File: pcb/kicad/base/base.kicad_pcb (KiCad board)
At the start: 2 copper layers, 59 parts, among them J1 CHIP_EN, J2 Vbatt_I-test, P1 J-Link SWD, P2 SMA, P3 Power Source, P4 CONN_01X08, U1 SAMB11G18A-edit, U2 XBee-PRO_900HP, Y1 32.768kHz, Y2 26MHz

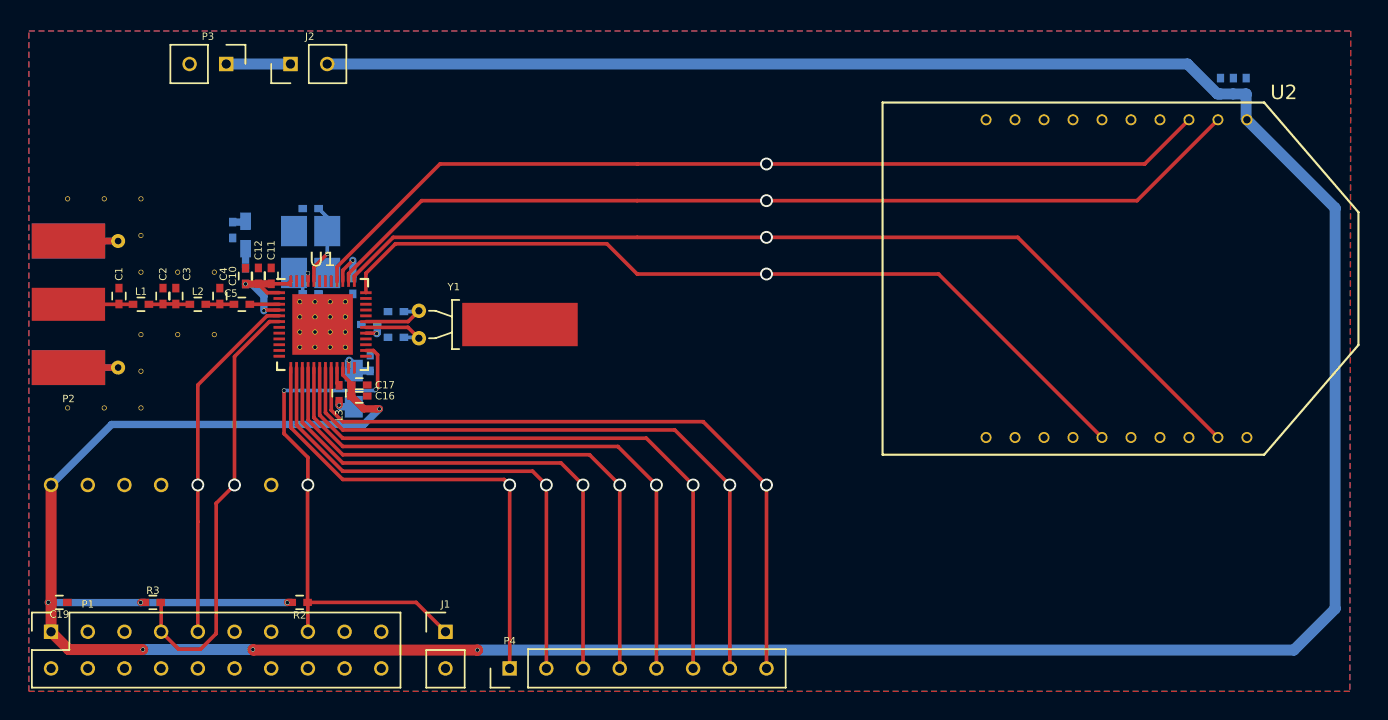
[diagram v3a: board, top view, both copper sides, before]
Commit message: Cleanup base schematic and layout
Power routes have been placed to completely cover the entire board.
Crystal adjusted slightly to avoid the UART TX signal line. More vias
dispersed around the board for better ground connections. Gerber files
have been created and are ready to be tiled.
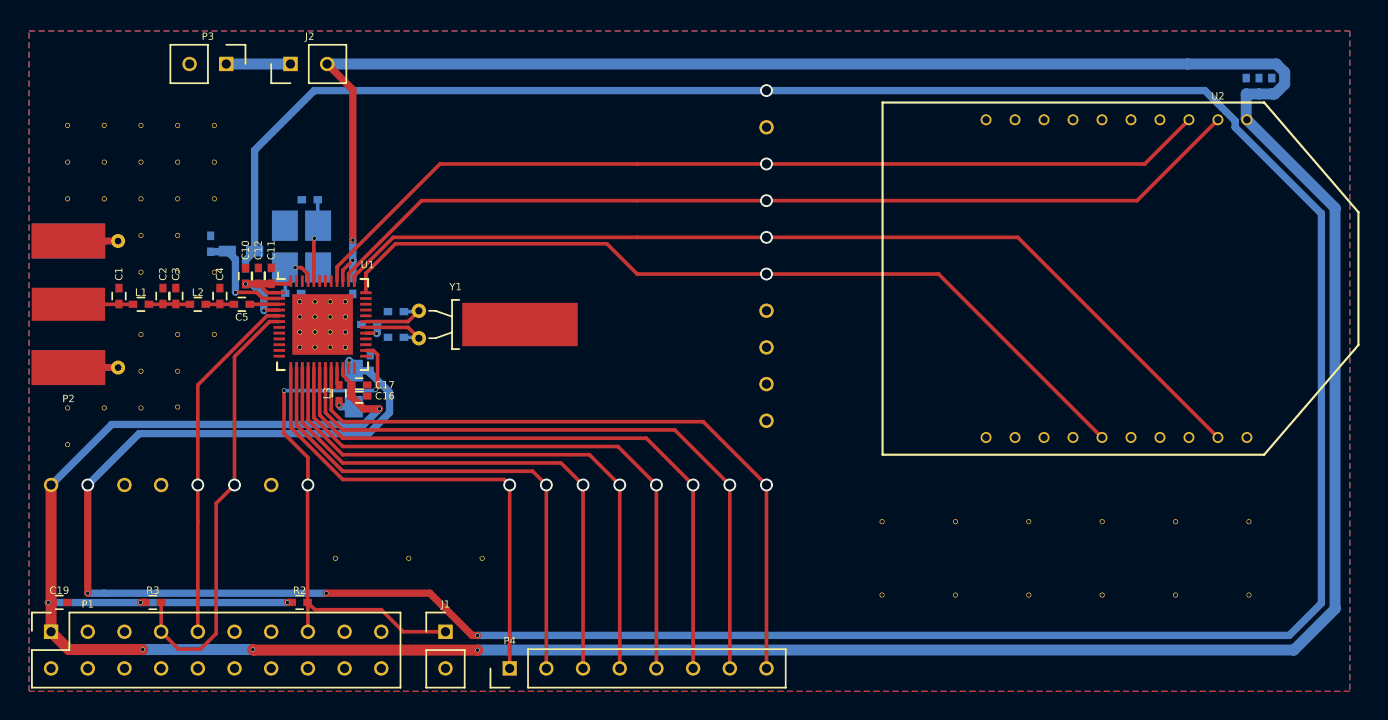
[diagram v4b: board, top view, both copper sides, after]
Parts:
- removed the REF** at (132.3, 100.0)
- added REF**: Via_Stitch_Dia0.356mm_Drill0.254mm, Misc:Via_Stitch_Dia0.356mm_Drill0.254mm, F.Cu at (138.6, 92.1)
- added REF**: Via_Stitch_Dia0.356mm_Drill0.254mm, Misc:Via_Stitch_Dia0.356mm_Drill0.254mm, F.Cu at (138.6, 94.6)
- added REF**: Via_Stitch_Dia0.356mm_Drill0.254mm, Misc:Via_Stitch_Dia0.356mm_Drill0.254mm, F.Cu at (138.6, 82.7)
- added REF**: Via_Stitch_Dia0.356mm_Drill0.254mm, Misc:Via_Stitch_Dia0.356mm_Drill0.254mm, F.Cu at (138.6, 80.2)
- added REF**: Via_Stitch_Dia1.00mm_Drill0.64mm, Misc:Via_Stitch_Dia1.00mm_Drill0.64mm, F.Cu at (179.3, 75.2)
- added REF**: Via_Stitch_Dia1.00mm_Drill0.64mm, Misc:Via_Stitch_Dia1.00mm_Drill0.64mm, F.Cu at (179.3, 87.9)
- added REF**: Via_Stitch_Dia1.00mm_Drill0.64mm, Misc:Via_Stitch_Dia1.00mm_Drill0.64mm, F.Cu at (179.3, 90.5)
- added REF**: Via_Stitch_Dia0.356mm_Drill0.254mm, Misc:Via_Stitch_Dia0.356mm_Drill0.254mm, F.Cu at (130.9, 97.2)
- added REF**: Via_Stitch_Dia0.356mm_Drill0.254mm, Misc:Via_Stitch_Dia0.356mm_Drill0.254mm, F.Cu at (130.9, 77.7)
- added REF**: Via_Stitch_Dia0.356mm_Drill0.254mm, Misc:Via_Stitch_Dia0.356mm_Drill0.254mm, F.Cu at (133.5, 77.7)
- added REF**: Via_Stitch_Dia0.356mm_Drill0.254mm, Misc:Via_Stitch_Dia0.356mm_Drill0.254mm, F.Cu at (136.0, 77.7)
- added REF**: Via_Stitch_Dia0.356mm_Drill0.254mm, Misc:Via_Stitch_Dia0.356mm_Drill0.254mm, F.Cu at (138.6, 77.7)
- added REF**: Via_Stitch_Dia0.356mm_Drill0.254mm, Misc:Via_Stitch_Dia0.356mm_Drill0.254mm, F.Cu at (141.1, 80.2)
- added REF**: Via_Stitch_Dia0.356mm_Drill0.254mm, Misc:Via_Stitch_Dia0.356mm_Drill0.254mm, F.Cu at (141.1, 77.7)
- added REF**: Via_Stitch_Dia0.356mm_Drill0.254mm, Misc:Via_Stitch_Dia0.356mm_Drill0.254mm, F.Cu at (130.9, 75.1)
- added REF**: Via_Stitch_Dia0.356mm_Drill0.254mm, Misc:Via_Stitch_Dia0.356mm_Drill0.254mm, F.Cu at (133.5, 75.1)
- added REF**: Via_Stitch_Dia0.356mm_Drill0.254mm, Misc:Via_Stitch_Dia0.356mm_Drill0.254mm, F.Cu at (136.0, 75.1)
- added REF**: Via_Stitch_Dia0.356mm_Drill0.254mm, Misc:Via_Stitch_Dia0.356mm_Drill0.254mm, F.Cu at (138.6, 75.1)
- added REF**: Via_Stitch_Dia0.356mm_Drill0.254mm, Misc:Via_Stitch_Dia0.356mm_Drill0.254mm, F.Cu at (141.1, 75.1)
- added REF**: Via_Stitch_Dia1.00mm_Drill0.64mm, Misc:Via_Stitch_Dia1.00mm_Drill0.64mm, F.Cu at (179.3, 93.0)
- added REF**: Via_Stitch_Dia1.00mm_Drill0.64mm, Misc:Via_Stitch_Dia1.00mm_Drill0.64mm, F.Cu at (179.3, 95.6)
- added REF**: Via_Stitch_Dia0.356mm_Drill0.254mm, Misc:Via_Stitch_Dia0.356mm_Drill0.254mm, F.Cu at (187.3, 107.6)
- added REF**: Via_Stitch_Dia0.356mm_Drill0.254mm, Misc:Via_Stitch_Dia0.356mm_Drill0.254mm, F.Cu at (192.4, 107.6)
- added REF**: Via_Stitch_Dia0.356mm_Drill0.254mm, Misc:Via_Stitch_Dia0.356mm_Drill0.254mm, F.Cu at (197.5, 107.6)
- added REF**: Via_Stitch_Dia0.356mm_Drill0.254mm, Misc:Via_Stitch_Dia0.356mm_Drill0.254mm, F.Cu at (202.6, 107.6)
- added REF**: Via_Stitch_Dia0.356mm_Drill0.254mm, Misc:Via_Stitch_Dia0.356mm_Drill0.254mm, F.Cu at (207.6, 107.6)
- added REF**: Via_Stitch_Dia0.356mm_Drill0.254mm, Misc:Via_Stitch_Dia0.356mm_Drill0.254mm, F.Cu at (212.7, 107.6)
- added REF**: Via_Stitch_Dia0.356mm_Drill0.254mm, Misc:Via_Stitch_Dia0.356mm_Drill0.254mm, F.Cu at (187.3, 102.6)
- added REF**: Via_Stitch_Dia0.356mm_Drill0.254mm, Misc:Via_Stitch_Dia0.356mm_Drill0.254mm, F.Cu at (192.4, 102.6)
- added REF**: Via_Stitch_Dia0.356mm_Drill0.254mm, Misc:Via_Stitch_Dia0.356mm_Drill0.254mm, F.Cu at (197.5, 102.6)
- added REF**: Via_Stitch_Dia0.356mm_Drill0.254mm, Misc:Via_Stitch_Dia0.356mm_Drill0.254mm, F.Cu at (202.6, 102.6)
- added REF**: Via_Stitch_Dia0.356mm_Drill0.254mm, Misc:Via_Stitch_Dia0.356mm_Drill0.254mm, F.Cu at (207.6, 102.6)
- added REF**: Via_Stitch_Dia0.356mm_Drill0.254mm, Misc:Via_Stitch_Dia0.356mm_Drill0.254mm, F.Cu at (212.7, 102.6)
- added REF**: Via_Stitch_Dia0.356mm_Drill0.254mm, Misc:Via_Stitch_Dia0.356mm_Drill0.254mm, F.Cu at (149.5, 105.1)
- added REF**: Via_Stitch_Dia0.356mm_Drill0.254mm, Misc:Via_Stitch_Dia0.356mm_Drill0.254mm, F.Cu at (154.6, 105.1)
- added REF**: Via_Stitch_Dia0.356mm_Drill0.254mm, Misc:Via_Stitch_Dia0.356mm_Drill0.254mm, F.Cu at (159.6, 105.1)
- moved C22 3.56 mm to (214.3, 72.4)
- moved C13 1.80 mm to (140.8, 83.3), turned to 90 degrees
- moved C21 1.78 mm to (213.4, 72.4)
- moved C9 1.21 mm to (146.6, 86.7)
- moved FB1 1.16 mm to (142.9, 83.8), turned to 180 degrees
- moved Y2 0.74 mm to (147.1, 83.5)
- moved C8 0.61 mm to (147.7, 80.3)
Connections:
- net /LP_GPIO_2 renamed Net-(U1-Pad7)
- net /LP_GPIO_22 renamed Net-(U1-Pad10)
- net /LP_GPIO_23 renamed Net-(U1-Pad11)
- net /LP_GPIO_3 renamed Net-(U1-Pad8)
- net /LP_GPIO_4 renamed Net-(U1-Pad9)
- net /LP_GPIO_5 renamed Net-(U1-Pad12)
- U1 pad 41: /LP_GPIO_18 -> GND
- U1 pad 42: /LP_GPIO_19 -> GND
- U1 pad 43: /LP_GPIO_20 -> GND
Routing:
- net Net-(C14-Pad1): track 3.89 -> 238.7 mm, vias 1 -> 6
- net /+3.3V: track 253.3 -> 273.4 mm, vias 8 -> 9
- net Net-(C13-Pad1): track 0.91 -> 7.46 mm, vias 0 -> 1
- net Net-(C9-Pad1): track 3.21 -> 4.08 mm
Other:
- rule pad_to_mask_clearance: 0.2 -> 0.0762
- board text added: "0.1"
- board text removed: "1.0"

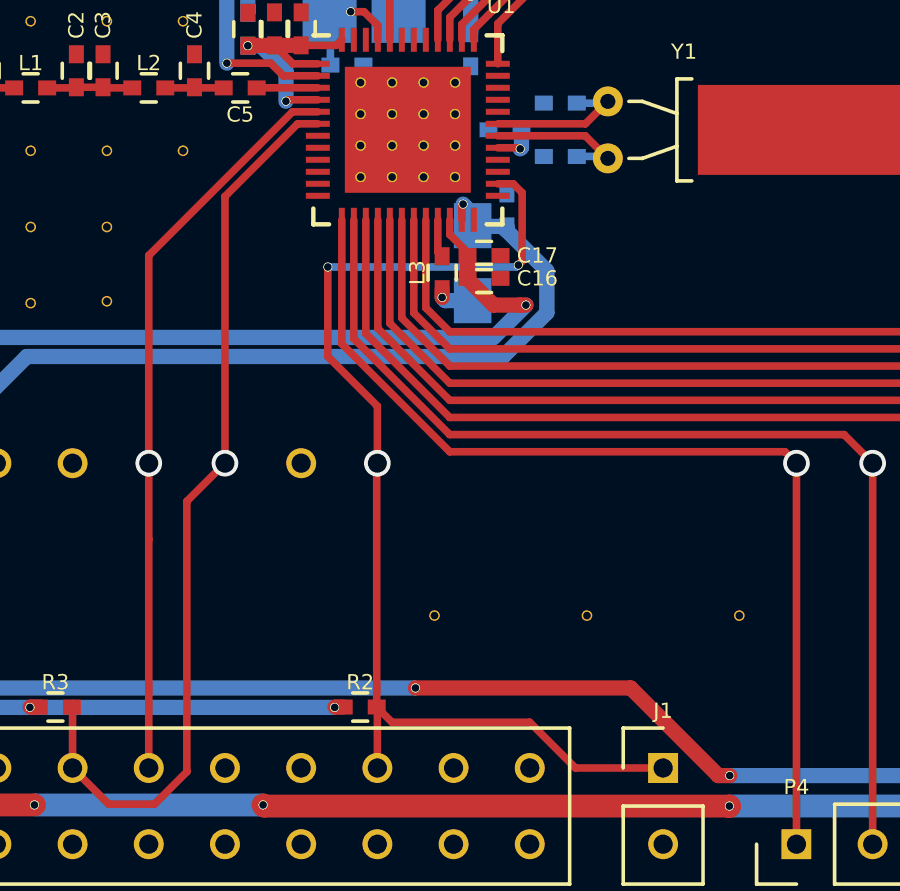
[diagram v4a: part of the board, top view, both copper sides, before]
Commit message: Fix annular ring clearance
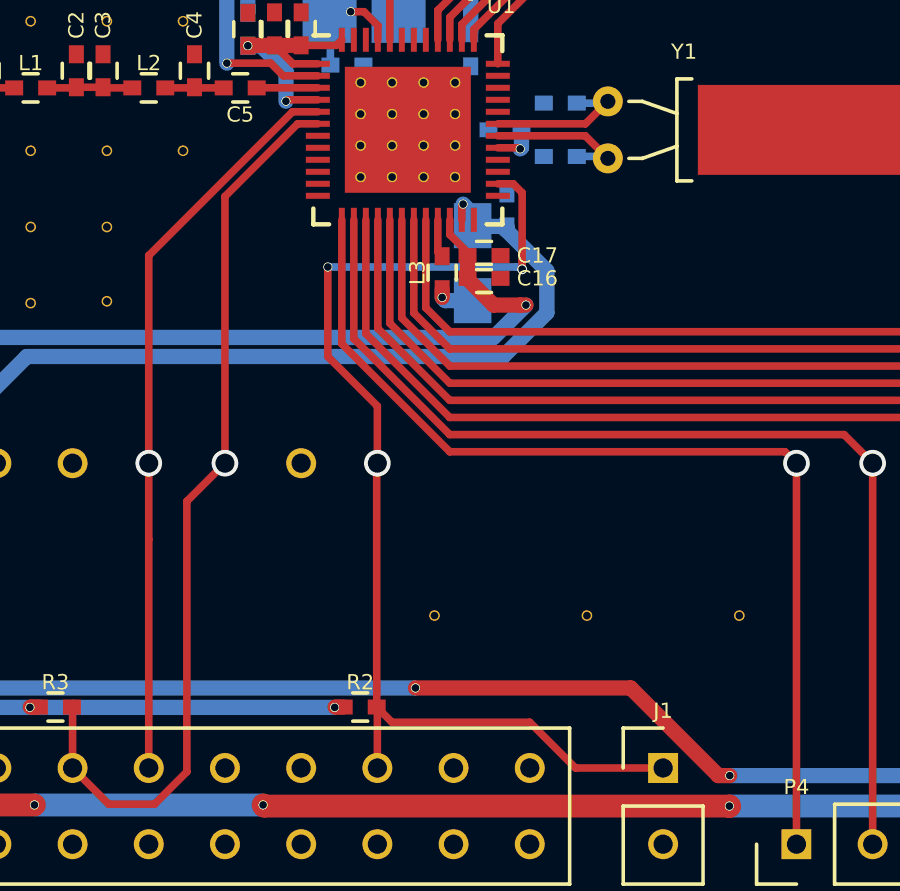
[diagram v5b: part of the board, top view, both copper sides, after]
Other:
- net class Default: via_dia 0.3048 -> 0.3302
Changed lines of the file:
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@@
-(kicad_pcb (version 4) (host pcbnew 4.0.5)
+(kicad_pcb (version 4) (host pcbnew 4.0.6)
   (general
     (links 200)
@@
     (thickness 1.6)
     (drawings 11)
-    (tracks 285)
+    (tracks 286)
     (zones 0)
     (modules 94)
@@
   )
   (setup
-    (last_trace_width 0.508)
+    (last_trace_width 0.254)
     (user_trace_width 0.508)
     (user_trace_width 0.762)
     (trace_clearance 0.127)
-    (zone_clearance 0.127)
+    (zone_clearance 0.1524)
     (zone_45_only yes)
     (trace_min 0.127)
     (segment_width 0.2)
     (edge_width 0.15)
-    (via_size 0.3048)
+    (via_size 0.3302)
     (via_drill 0.254)
     (via_min_size 0.254)
     (via_min_drill 0.254)
+    (user_via 0.3302 0.254)
     (user_via 0.889 0.635)
     (uvia_size 0.3)
@@
       (drillshape 0)
       (scaleselection 1)
-      (outputdirectory ""))
+      (outputdirectory artwork/))
   )
   (net 0 "")
@@
     (clearance 0.127)
     (trace_width 0.254)
-    (via_dia 0.3048)
+    (via_dia 0.3302)
     (via_drill 0.254)
     (uvia_dia 0.3)
@@
   (segment (start 149.84 94.595) (end 149.733 94.488) (width 0.508) (layer B.Cu) (net 45))
   (segment (start 150.749 94.595) (end 149.84 94.595) (width 0.508) (layer B.Cu) (net 45))
+  (segment (start 152.4 93.2815) (end 152.4 93.5482) (width 0.254) (layer F.Cu) (net 52))
+  (via (at 152.4 93.5482) (size 0.3302) (drill 0.254) (layers F.Cu B.Cu) (net 52))
+  (segment (start 152.3238 93.472) (end 152.4 93.5482) (width 0.254) (layer B.Cu) (net 52))
+  (segment (start 152.2095 93.472) (end 152.3238 93.472) (width 0.254) (layer B.Cu) (net 52))
+  (segment (start 152.1045 90.7) (end 152.4 90.9955) (width 0.254) (layer F.Cu) (net 52))
+  (segment (start 152.4 90.9955) (end 152.4 93.2815) (width 0.254) (layer F.Cu) (net 52))
+  (segment (start 151.59 90.7) (end 152.1045 90.7) (width 0.254) (layer F.Cu) (net 52))
+  (segment (start 152.2095 93.472) (end 145.923 93.472) (width 0.254) (layer B.Cu) (net 52))
+  (segment (start 147.574 98.1075) (end 145.923 96.4565) (width 0.254) (layer F.Cu) (net 52))
+  (segment (start 145.923 96.4565) (end 145.923 93.472) (width 0.254) (layer F.Cu) (net 52))
+  (via (at 145.923 93.472) (size 0.3048) (drill 0.254) (layers F.Cu B.Cu) (net 52))
+  (segment (start 147.5525 100.034) (end 147.5525 108.1405) (width 0.254) (layer F.Cu) (net 52))
+  (via (at 147.574 100.0125) (size 0.889) (drill 0.635) (layers F.Cu B.Cu) (net 52))
+  (segment (start 147.5525 100.034) (end 147.574 100.0125) (width 0.254) (layer F.Cu) (net 52))
+  (segment (start 147.574 100.0125) (end 147.574 98.1075) (width 0.254) (layer F.Cu) (net 52))
   (segment (start 148.0605 108.6485) (end 147.5525 108.1405) (width 0.254) (layer F.Cu) (net 52))
   (segment (start 152.654 108.6485) (end 148.0605 108.6485) (width 0.254) (layer F.Cu) (net 52))
   (segment (start 154.178 110.1725) (end 152.654 108.6485) (width 0.254) (layer F.Cu) (net 52))
   (segment (start 157.099 110.1725) (end 154.178 110.1725) (width 0.254) (layer F.Cu) (net 52))
-  (segment (start 147.574 100.0125) (end 147.574 98.1075) (width 0.254) (layer F.Cu) (net 52))
-  (segment (start 147.5525 100.034) (end 147.574 100.0125) (width 0.254) (layer F.Cu) (net 52))
-  (via (at 147.574 100.0125) (size 0.889) (drill 0.635) (layers F.Cu B.Cu) (net 52))
-  (segment (start 147.5525 108.1405) (end 147.5525 100.034) (width 0.254) (layer F.Cu) (net 52))
-  (segment (start 152.1045 90.7) (end 152.4 90.9955) (width 0.254) (layer F.Cu) (net 52))
-  (segment (start 152.4 90.9955) (end 152.4 93.2815) (width 0.254) (layer F.Cu) (net 52))
-  (segment (start 152.4 93.2815) (end 152.273 93.4085) (width 0.254) (layer F.Cu) (net 52))
-  (via (at 152.273 93.4085) (size 0.3048) (drill 0.254) (layers F.Cu B.Cu) (net 52))
-  (segment (start 152.273 93.4085) (end 152.2095 93.472) (width 0.254) (layer B.Cu) (net 52))
-  (segment (start 152.2095 93.472) (end 145.923 93.472) (width 0.254) (layer B.Cu) (net 52))
-  (via (at 145.923 93.472) (size 0.3048) (drill 0.254) (layers F.Cu B.Cu) (net 52))
-  (segment (start 152.1045 90.7) (end 151.59 90.7) (width 0.254) (layer F.Cu) (net 52))
-  (segment (start 145.923 96.4565) (end 145.923 93.472) (width 0.254) (layer F.Cu) (net 52))
-  (segment (start 147.574 98.1075) (end 145.923 96.4565) (width 0.254) (layer F.Cu) (net 52))
   (segment (start 147.574 110.1725) (end 147.574 108.162) (width 0.254) (layer F.Cu) (net 52))
   (segment (start 147.574 108.162) (end 147.5525 108.1405) (width 0.254) (layer F.Cu) (net 52))
@@
   (segment (start 141.9225 70.866) (end 146.3675 70.866) (width 0.762) (layer B.Cu) (net 57))
   (zone (net 2) (net_name GND) (layer F.Cu) (hatch edge 0.508)
-    (connect_pads thru_hole_only (clearance 0.127))
-    (min_thickness 0.127)
+    (connect_pads thru_hole_only (clearance 0.1524))
+    (min_thickness 0.1524)
     (fill yes (mode segment) (arc_segments 16) (thermal_gap 0.508) (thermal_bridge_width 0.508))
     (polygon
@@
   )
   (zone (net 2) (net_name GND) (layer B.Cu) (hatch edge 0.508)
-    (connect_pads thru_hole_only (clearance 0.127))
-    (min_thickness 0.127)
+    (connect_pads thru_hole_only (clearance 0.1524))
+    (min_thickness 0.1524)
     (fill yes (mode segment) (arc_segments 16) (thermal_gap 0.508) (thermal_bridge_width 0.508))
     (polygon
